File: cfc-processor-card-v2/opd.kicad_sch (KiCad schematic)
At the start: 96 parts, among them Q2 PMV45EN, Q3 DMP2240UDM, Q4 PMV45EN, Q5 MOSFET-PCH-SOT23-6, Q6 MOSFET-PCH-SOT23-6, U12 MIC842LYC5, U13 MIC842LYC5, U14 MAX4211FETE, U15 TPS62112, U16 MAX7310ATE, U5 TS5A21366

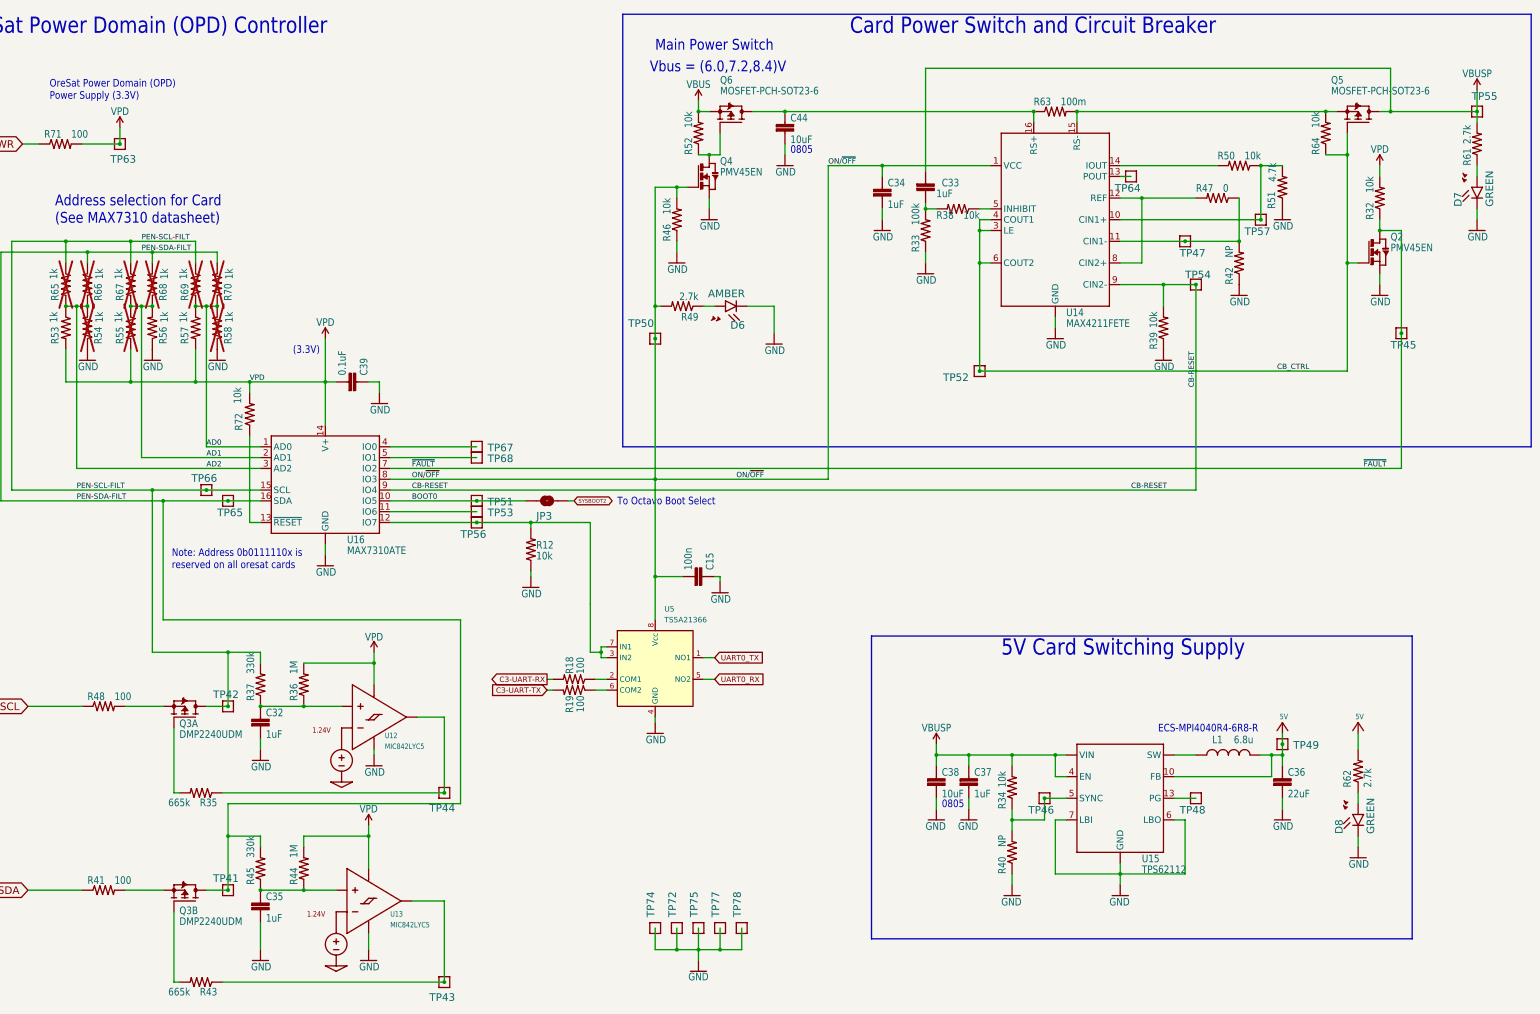
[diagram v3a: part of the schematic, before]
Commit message: Final polish on schematic and PCB. Cleaned up BOM, fixed github issues which were not really issues. Lots of BOM cleanup, with MPNs and DPNs.
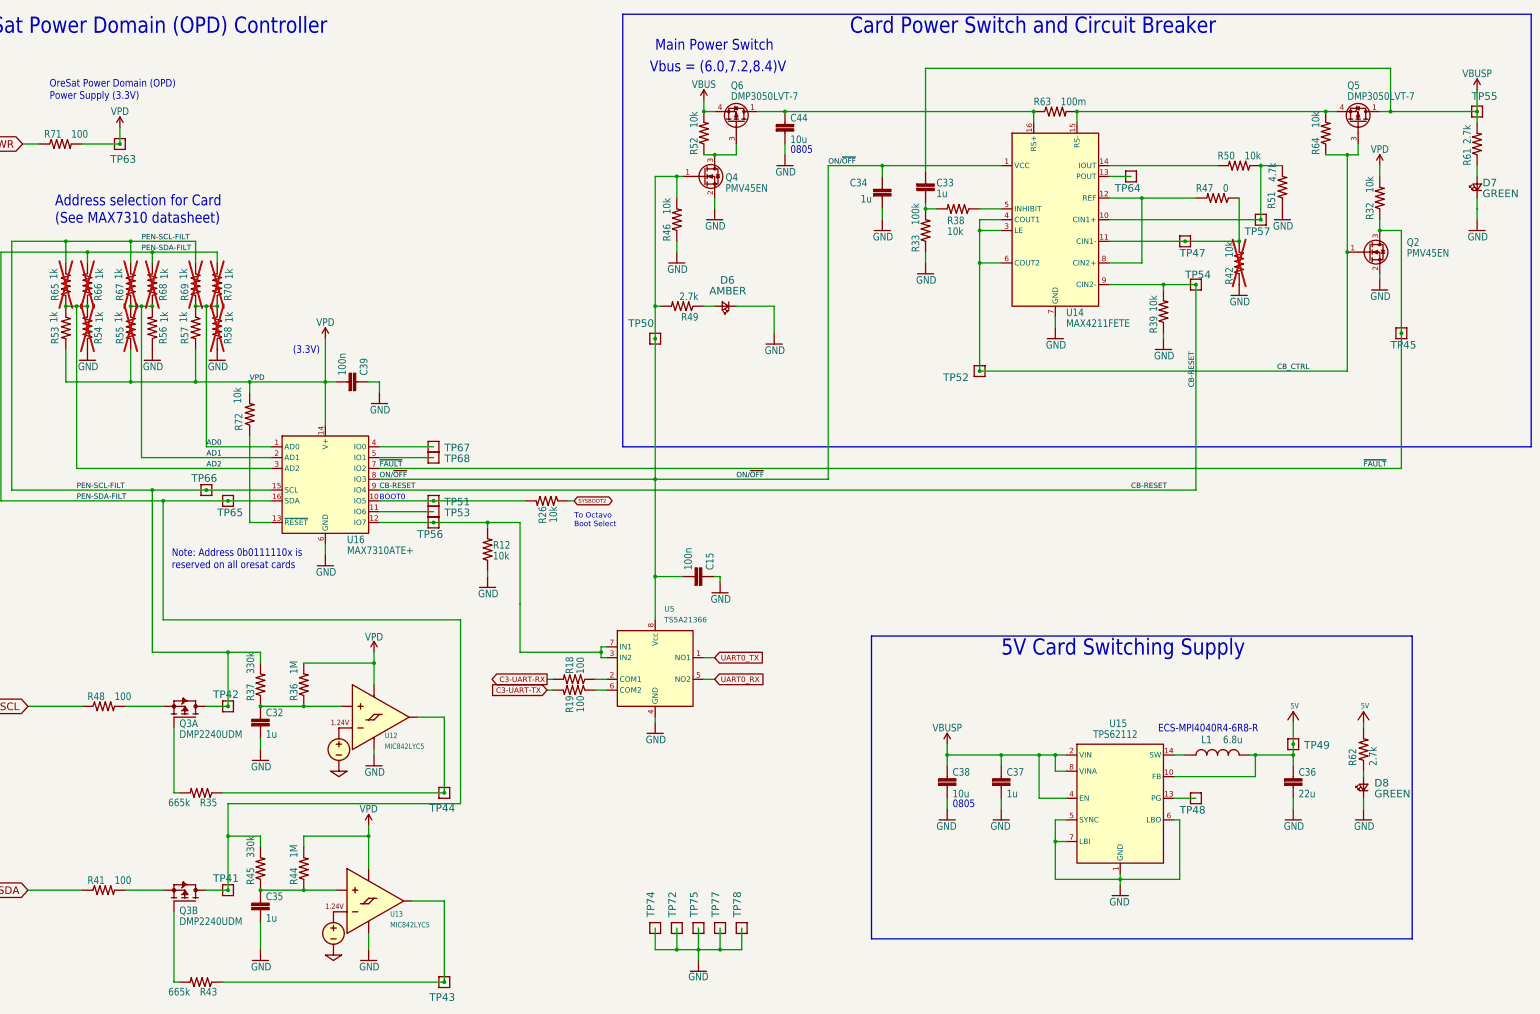
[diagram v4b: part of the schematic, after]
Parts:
- removed JP3: JUMPER-SMT_2_NO_SILK, cfc-card:SMT-JUMPER_2_NO_SILK, symbol cfc-card-eagle-import:JUMPER-SMT_2_NO_SILK
- removed R34: 10k, oresat-passives:0603-C-NOSILK, symbol cfc-card-eagle-import:R-US_0603-A
- removed R40: NP, oresat-passives:0603-C-NOSILK, symbol cfc-card-eagle-import:R-US_0603-A
- removed TP46: TEST-POINT, cfc-card:2MM-TEST-POINT, symbol cfc-card-eagle-import:TEST-POINT
- added R26: 10k, oresat-passives:0603-C-NOSILK, symbol cfc-card-eagle-import:R-US_0603-A
- C15: DIS (none) -> DigiKey; DPN (none) -> 587-3472-1-ND; MFR (none) -> Taiyo Yuden; MPN (none) -> TMK107BJ104KAHT
- C32, C35: value 1uF -> 1u; footprint oresat-passives:0805-C-NOSILK -> oresat-passives:0603-C-NOSILK; DIS (none) -> DigiKey; DPN (none) -> 587-3473-1-ND; MFR (none) -> Taiyo Yuden; MPN (none) -> TMK107BJ105KAHT
- C33: value 1uF -> 1u; DIS Digi-Key -> DigiKey; DPN 1276-1001-1-ND -> 587-3473-1-ND; MFR Samsung -> Taiyo Yuden; MPN (none) -> TMK107BJ105KAHT
- C34, C37: value 1uF -> 1u; DIS (none) -> DigiKey; DPN (none) -> 587-3473-1-ND; MFR (none) -> Taiyo Yuden; MPN (none) -> TMK107BJ105KAHT
- C36: value 22uF -> 22u; footprint cfc-card:C1210 -> Capacitor_SMD:C_1210_3225Metric; DIS (none) -> DigiKey; DPN (none) -> 490-GCM32EC71E226KE36KCT-ND; MFR (none) -> Murata Electronics; MPN (none) -> GCM32EC71E226KE36K
- C38, C44: value 10uF -> 10u; DIS (none) -> DigiKey; DPN (none) -> 490-GRT21BC71E106KE13LCT-ND; MFR (none) -> Murata Electronics; MPN (none) -> GRT21BC71E106KE13L
- C39: value 0.1uF -> 100n; DIS (none) -> DigiKey; DPN (none) -> 587-3472-1-ND; MFR (none) -> Taiyo Yuden; MPN (none) -> TMK107BJ104KAHT
- D6: footprint cfc-card:LED-0603 -> LED_SMD:LED_0603_1608Metric; symbol cfc-card-eagle-import:SparkFun-LED_529_LED-GREEN0603 -> Device:LED_Small; DIS (none) -> DigiKey; DPN (none) -> 732-150060AS75000CT-ND; MFR (none) -> Wurth; MPN (none) -> 150060AS75000
- D7, D8: footprint cfc-card:LED-0603 -> LED_SMD:LED_0603_1608Metric; symbol cfc-card-eagle-import:LED-GREEN0603 -> Device:LED_Small; DIS (none) -> DigiKey; DPN (none) -> 732-4971-1-ND; MFR (none) -> Wurth; MPN (none) -> 150060GS75000
- L1: footprint cfc-card:ECS-MPI4040 -> oresat-passives:L_ECS-MPI4040; DIS (none) -> DigiKey; DPN (none) -> XC2337CT-ND; MFR (none) -> ECS Inc.; MPN (none) -> ECS-MPI4040R4-6R8-R
- Q2, Q4: footprint cfc-card:SOT23 -> Package_TO_SOT_SMD:SOT-23-3; symbol cfc-card-eagle-import:PMV45EN -> Transistor_FET:Q_NMOS_GSD; DIS (none) -> DigiKey; MFR (none) -> Nexperia
- Q3: footprint cfc-card:SOT23-6 -> Package_TO_SOT_SMD:SOT-23-6; DIS (none) -> DigiKey; DPN (none) -> DMP2240UDMDICT-ND; MFR (none) -> Diodes Inc; MPN (none) -> DMP2240UDM
- Q5, Q6: value MOSFET-PCH-SOT23-6 -> DMP3050LVT-7; footprint cfc-card:SOT23-6 -> Package_TO_SOT_SMD:TSOT-23-6; symbol cfc-card-eagle-import:MOSFET-PCH-SOT23-6 -> oresat-transistors:DMP3050LVT-7; DIS (none) -> DigiKey; DPN (none) -> DMP3050LVT-7DICT-ND; MFR (none) -> Diodes Inc
- R12, R32, R39, R46, R50, R52, R64, R72: DIS (none) -> DigiKey; DPN (none) -> RMCF0603FT10K0CT-ND; MFR (none) -> Stackpole Electronics Inc; MPN (none) -> RMCF0603FT10K0
- R18, R19, R41, R48, R71: DIS (none) -> DigiKey; DPN (none) -> RMCF0603FT100RCT-ND; MFR (none) -> Stackpole Electronics Inc; MPN (none) -> RMCF0603FT100R
- R33: DIS Digi-Key -> DigiKey; DPN 1276-4275-1-ND -> RMCF0603FT100KCT-ND; MFR Samsung -> Stackpole Electronics Inc; MPN RC1005F6653CS -> RMCF0603FT100K
- R35, R43: DIS (none) -> DigiKey; DPN (none) -> RMCF0603FT665KCT-ND; MFR (none) -> Stackpole Electronics Inc; MPN (none) -> RMCF0603FT665K
- R36, R44: DIS (none) -> DigiKey; DPN (none) -> RMCF0603FG1M00CT-ND; MFR (none) -> Stackpole Electronics Inc; MPN (none) -> RMCF0603FG1M00
- R37, R45: DIS (none) -> DigiKey; DPN (none) -> RMCF0603FT330KCT-ND; MFR (none) -> Stackpole Electronics Inc; MPN (none) -> RMCF0603FT330K
- R38: DIS Digi-Key -> DigiKey; DPN 1276-4275-1-ND -> RMCF0603FT10K0CT-ND; MFR Samsung -> Stackpole Electronics Inc; MPN RC1005F6653CS -> RMCF0603FT10K0
- R42: value NP -> 10k; now not fitted
- R47: DIS (none) -> DigiKey; DPN (none) -> RMCF0603ZT0R00CT-ND; MFR (none) -> Stackpole Electronics Inc; MPN (none) -> RMCF0603ZT0R00
- R49, R61, R62: DIS (none) -> DigiKey; DPN (none) -> RMCF0603FT2K70CT-ND; MFR (none) -> Stackpole Electronics Inc; MPN (none) -> RMCF0603FT2K70
- R51: DIS Digi-Key -> DigiKey; DPN 1276-4275-1-ND -> RMCF0603FT4K70CT-ND; MFR Samsung -> Stackpole Electronics Inc; MPN RC1005F6653CS -> RMCF0603FT4K70
- R53, R56, R57: DIS Digi-Key -> DigiKey; DPN 1276-4275-1-ND -> RMCF0603FT1K00CT-ND; MFR Samsung -> Stackpole Electronics Inc; MPN RC1005F6653CS -> RMCF0603FT1K00
- R63: DIS (none) -> DigiKey; DPN (none) -> CSR1206FTR100CT-ND; MFR (none) -> Stackpole Electronics Inc; MPN (none) -> CSR1206FTR100
- TP41, TP42, TP43, TP44, TP45, TP47, TP48, TP49, TP50, TP51, TP52, TP53, TP54, TP55, TP56, TP57, TP63, TP64, TP65, TP66, TP67, TP68, TP72, TP74, TP75, TP77, TP78: now left out of the parts list
- U12, U13: footprint cfc-card:SC70-5 -> Package_TO_SOT_SMD:SOT-353_SC-70-5; symbol cfc-card-eagle-import:MIC842LYC5 -> oresat-ics:MIC842LYC5; DIS (none) -> DigiKey; DPN (none) -> 576-2927-1-ND; MFR (none) -> Microchip Technology; MPN (none) -> MIC842LYC5-TR
- U14: footprint cfc-card:QFN65P400X400X80-17T210 -> Package_DFN_QFN:QFN-16-1EP_4x4mm_P0.65mm_EP2.1x2.1mm; symbol cfc-card-eagle-import:MAX4211 -> oresat-ics:MAX4211FETE; DIS (none) -> DigiKey; DPN (none) -> MAX4211FETE+-ND; MFR (none) -> Analog Devices; MPN (none) -> MAX4211FETE
- U15: footprint cfc-card:S-PVQFN-16 -> Package_DFN_QFN:Texas_RSA_VQFN-16-1EP_4x4mm_P0.65mm_EP2.7x2.7mm; symbol cfc-card-eagle-import:TPS6211X -> oresat-ics:TPS6211X; DIS (none) -> DigiKey; DPN (none) -> 296-39444-1-ND; MFR (none) -> Texas Instruments; MPN (none) -> TPS62112RSAR
- U16: value MAX7310ATE -> MAX7310ATE+; footprint cfc-card:QFN65P400X400X80-17T210 -> Package_DFN_QFN:QFN-16-1EP_4x4mm_P0.65mm_EP2.1x2.1mm; symbol cfc-card-eagle-import:MAX7310 -> oresat-ics:MAX7310; DIS (none) -> DigiKey; DPN (none) -> MAX7310ATE+-ND; MFR Maxim -> Analog Devices; MPN MAX7310ATE -> MAX7310ATE+
- U5: DIS (none) -> DigiKey; DPN (none) -> 296-24304-1-ND; MFR (none) -> Texas Instruments; MPN (none) -> TS5A21366DCUR
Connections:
- net GND: now also D6.1 (K), D7.1 (K), D8.1 (K), U14.17 (GND), U15.17 (GND), U15.5 (SYNC), U16.17 (GND); no longer D6.C, D7.C, D8.C, U14.EPAD (GND), U15.PAD (GND), U16.EPAD (GND)
- net SYSBOOT2: now also R26.1
- net at R62.1: now also D8.2 (A); no longer D8.A
- net at R49.1: now also D6.2 (A); no longer D6.A
- net at R61.1: now also D7.2 (A); no longer D7.A
- net BOOT0: no longer names the net of TP51.1, U16.10 (IO5)
- net BOOT0: now also R26.2
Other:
- note added: "BOOT0"
- moved on the sheet: C36, C37, C38, L1, R12, R39, R52, R62, TP49, TP51, TP53, TP56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
